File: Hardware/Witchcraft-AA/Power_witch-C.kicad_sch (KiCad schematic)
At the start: 13 parts, among them J2 TE_2129567-1, J3 Conn_01x05_Socket, J5 Conn_01x02_Socket, U1 Z1 extreme, U2 LM26420-Q1xx-xxxx, U3 K3LKCKC0BM, U4 K3LKCKC0BM

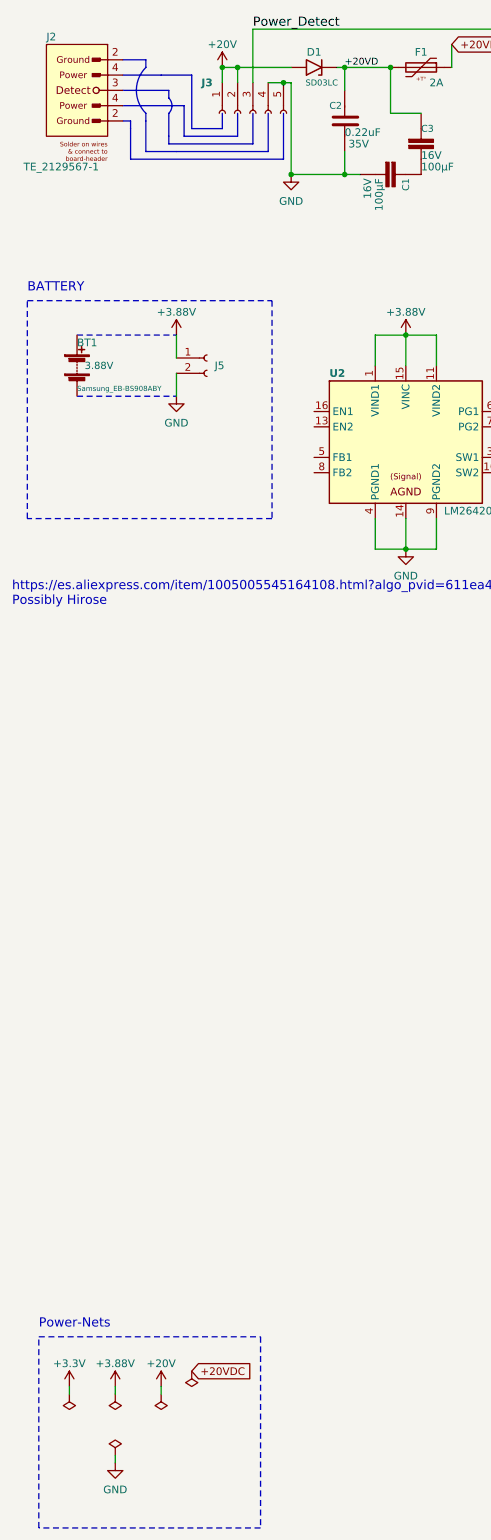
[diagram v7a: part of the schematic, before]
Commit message: Upgraded the shell-assembly to the Assembly4 workbench, allowing for better performance.
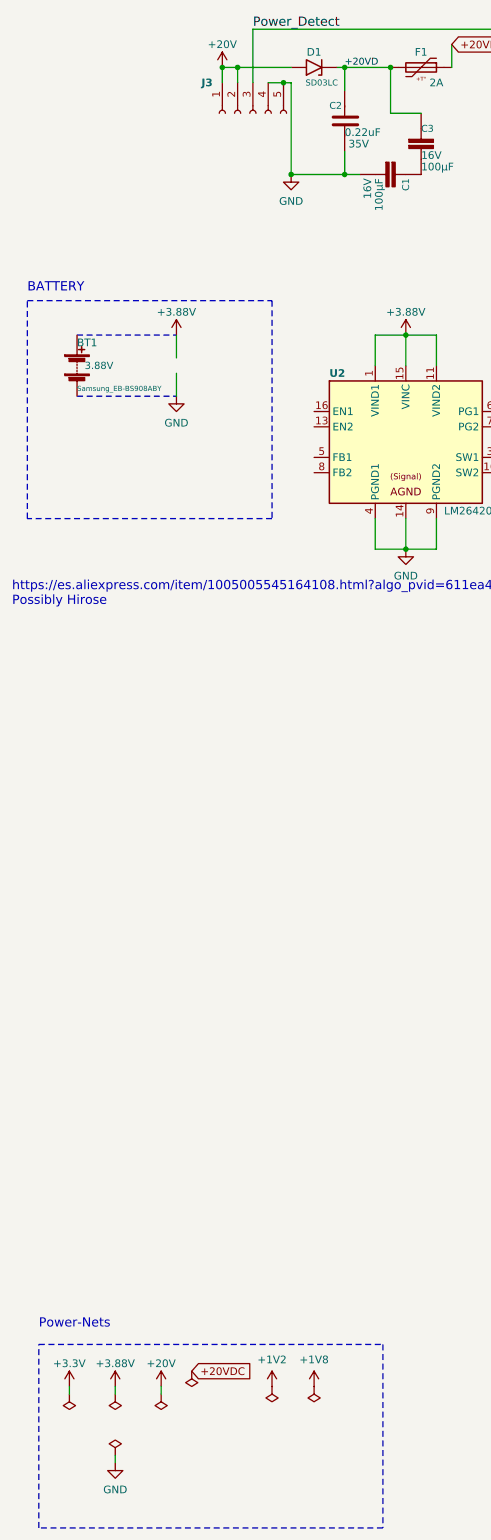
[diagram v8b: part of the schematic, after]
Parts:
- removed J2: TE_2129567-1, LRJ:TE_2129567-1, symbol LRJ-parts:TE_2129567-1
- removed J5: Conn_01x02_Socket, symbol Connector:Conn_01x02_Socket
